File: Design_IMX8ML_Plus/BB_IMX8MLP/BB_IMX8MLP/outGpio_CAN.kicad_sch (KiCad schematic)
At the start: 21 parts, among them J24 CAN_1, J25 CAN_2, U33 ISO1044BD, U38 ISO1044BD, U42 NTE0505MC, U43 NTE0505MC

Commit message: CPU Board actualizate
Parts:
- U42, U43: footprint _W_SBC:NTE_SINGLE_M_MUR-L -> NTE_SINGLE_M_MUR
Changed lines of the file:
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@@
 	)
 	(symbol
-		(lib_name "NTE0505MC_1")
 		(lib_id "NTE0505MEC-R:NTE0505MC")
 		(at 157.48 45.72 0)
@@
 			)
 		)
-		(property "Footprint" "_W_SBC:NTE_SINGLE_M_MUR-L"
+		(property "Footprint" "NTE_SINGLE_M_MUR"
 			(at 163.83 64.77 90)
 			(effects
@@
 	)
 	(symbol
-		(lib_name "NTE0505MC_1")
 		(lib_id "NTE0505MEC-R:NTE0505MC")
 		(at 80.01 172.72 0)
@@
 			)
 		)
-		(property "Footprint" "_W_SBC:NTE_SINGLE_M_MUR-L"
+		(property "Footprint" "NTE_SINGLE_M_MUR"
 			(at 86.36 191.77 90)
 			(effects

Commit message: [PROCESSOR] Create zones It added power zones in the four layer
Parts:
- added U39: ~, Package_TO_SOT_SMD:SOT-23-3, symbol _W_MX8M:PESD2IVN24-T
- J24, J25: footprint Connector_PinSocket_2.54mm:PinSocket_1x04_P2.54mm_Vertical -> Connector_Phoenix_MSTB:PhoenixContact_MSTBA_2,5_4-G_1x04_P5.00mm_Horizontal
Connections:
- net GND_CAN1: now also U39.3
- net at J24.3 (Pin_3), U38.6 (CANH): now also U39.2
- net at J24.4 (Pin_4), U38.5 (CANL): now also U39.1
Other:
- moved on the sheet: C161, C162, C167, C168, C169, C178, C179, C180, C187, J25, R17, U33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

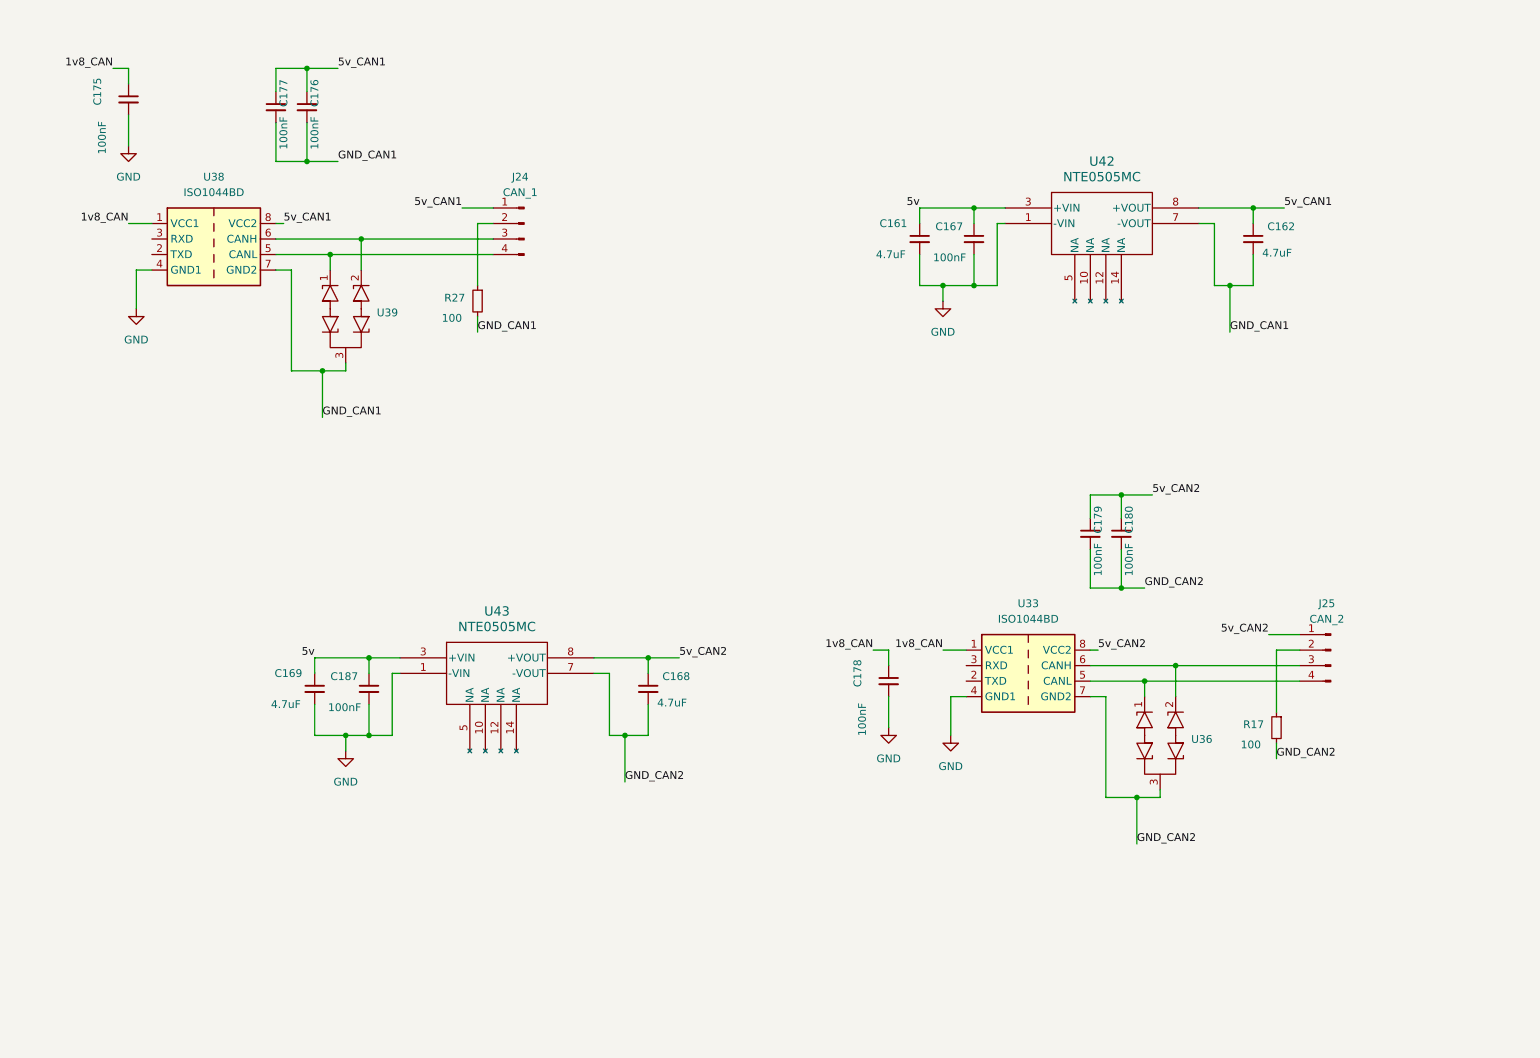
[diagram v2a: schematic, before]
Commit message: [BB_IMX8MLP IMX8MLP] Actuallizated to 9.0 kicad version
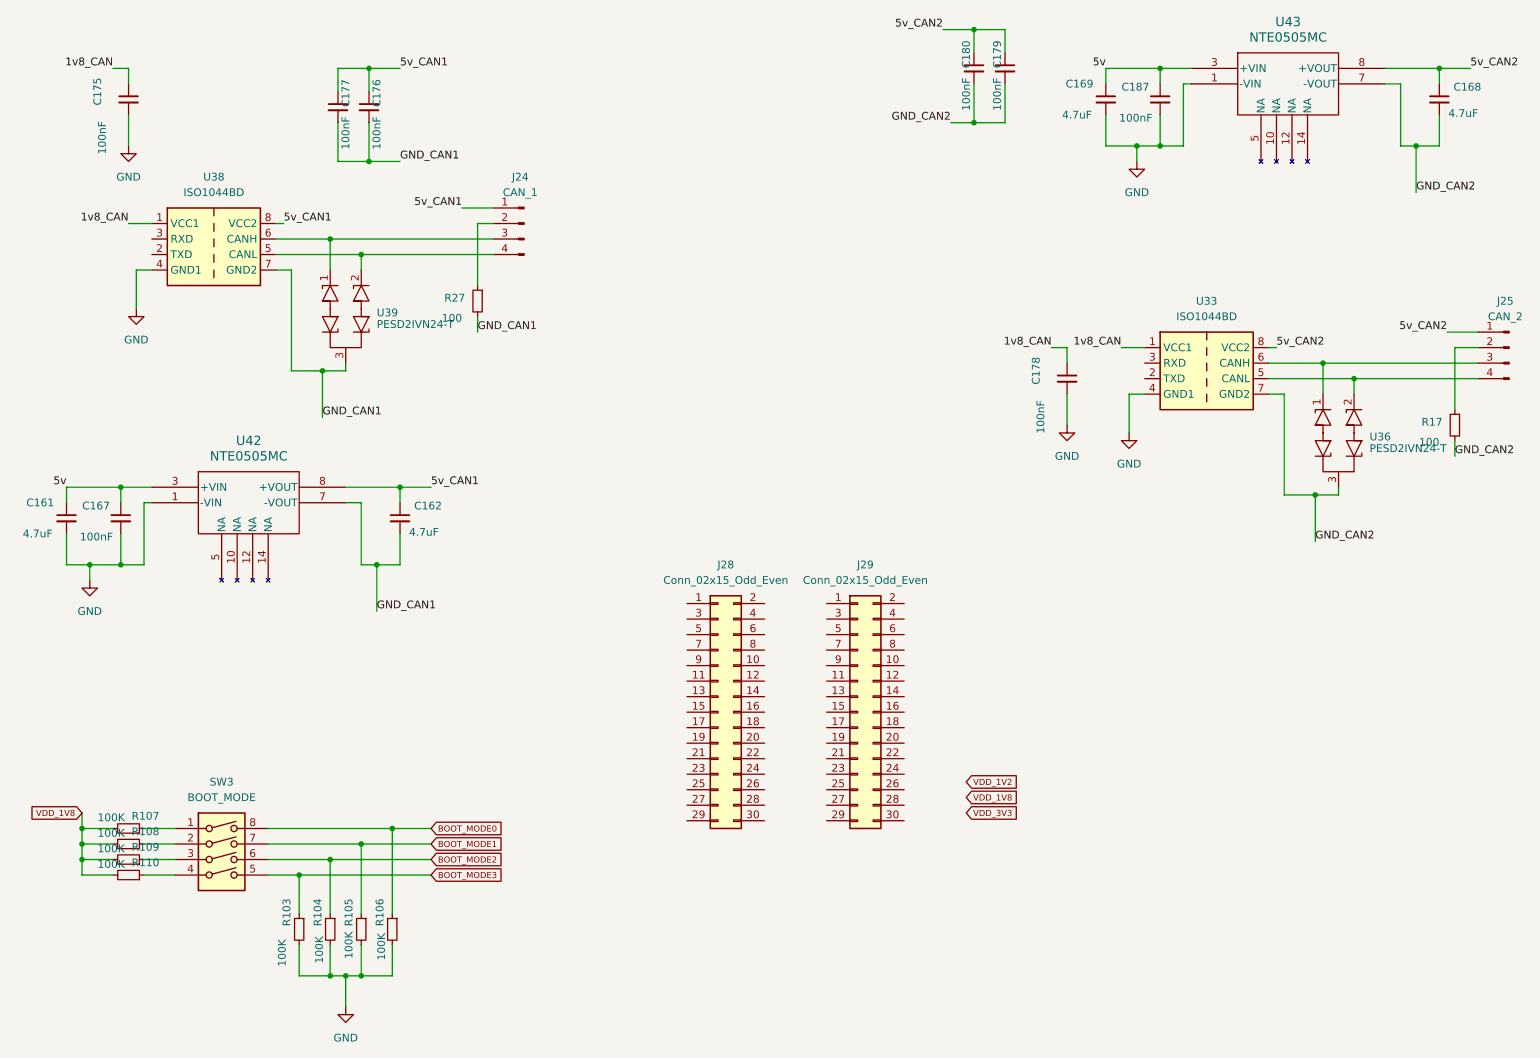
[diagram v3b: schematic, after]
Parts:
- added J28, J29: Conn_02x15_Odd_Even, Connector_PinHeader_2.54mm:PinHeader_2x16_P2.54mm_Vertical, symbol Connector_Generic:Conn_02x15_Odd_Even
- added R103, R104, R105, R106, R107, R108, R109, R110: 100K, Resistor_SMD:R_0402_1005Metric, symbol Device:R_Small
- added SW3: BOOT_MODE, Button_Switch_THT:SW_DIP_SPSTx04_Slide_9.78x12.34mm_W7.62mm_P2.54mm, symbol Switch:SW_DIP_x04
- C161, C162, C168, C169: MP (none) -> CL05A475KQ5NRNC; Price (none) -> 0.1
- C167, C175, C176, C177, C178, C179, C180, C187: MP (none) -> C0402C104K4RACTU; Price (none) -> 0.1
- R17, R27: MP (none) -> RC0402JR-07100RL; Price (none) -> 0.1
- U33, U38: MP (none) -> ISO1044BD; Price (none) -> 4
- U36, U39: value ~ -> PESD2IVN24-T; MP (none) -> PESD2IVN24-T; Price (none) -> 0.5
- U42, U43: MP (none) -> NTE0505MC; Price (none) -> 8
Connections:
- net GND: now also R103.2, R104.2, R105.2, R106.2
- net at J25.3 (Pin_3), U33.6 (CANH): now also U36.1; no longer U36.2
- net at J25.4 (Pin_4), U33.5 (CANL): now also U36.2; no longer U36.1
- net at J24.3 (Pin_3), U38.6 (CANH): now also U39.1; no longer U39.2
- net at J24.4 (Pin_4), U38.5 (CANL): now also U39.2; no longer U39.1
- new net: R107.1, SW3.1
- new net: R108.1, SW3.2
- new net: R109.1, SW3.3
- new net: R110.1, SW3.4
- new net BOOT_MODE0: R106.1, SW3.8
- new net BOOT_MODE1: R105.1, SW3.7
- new net BOOT_MODE2: R104.1, SW3.6
- new net BOOT_MODE3: R103.1, SW3.5
- new net VDD_1V8: R107.2, R108.2, R109.2, R110.2
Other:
- moved on the sheet: C161, C162, C167, C168, C169, C176, C177, C178, C179, C180, C187, J25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

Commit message: [BB_IMX8ML] It was reoganizated the device position
It was reorganized the devices to improve the routing.
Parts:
- J24, J25: footprint Connector_Phoenix_MSTB:PhoenixContact_MSTBA_2,5_4-G_1x04_P5.00mm_Horizontal -> Connector_PinSocket_2.54mm:PinSocket_1x04_P2.54mm_Vertical
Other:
- moved on the sheet: C161, C162, C167, C168, C169, C175, C176, C177, C178, C179, C180, C187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

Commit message: [IMX8ML] Add new layer
A new layers was add in the cpu schematic, now it had 8 layer.
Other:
- moved on the sheet: J28, J29, R103, R104, R105, R106, R107, R108, R109, R110, SW3
